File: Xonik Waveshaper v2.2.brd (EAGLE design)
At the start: 55.9 x 21 mm, 78 parts, among them IC1 TL074JT, IC2 TL074JT, IC3 TL074JT, IC4 TL072JT, IC5 4013T, IC6 LM311T, T1 2n3904

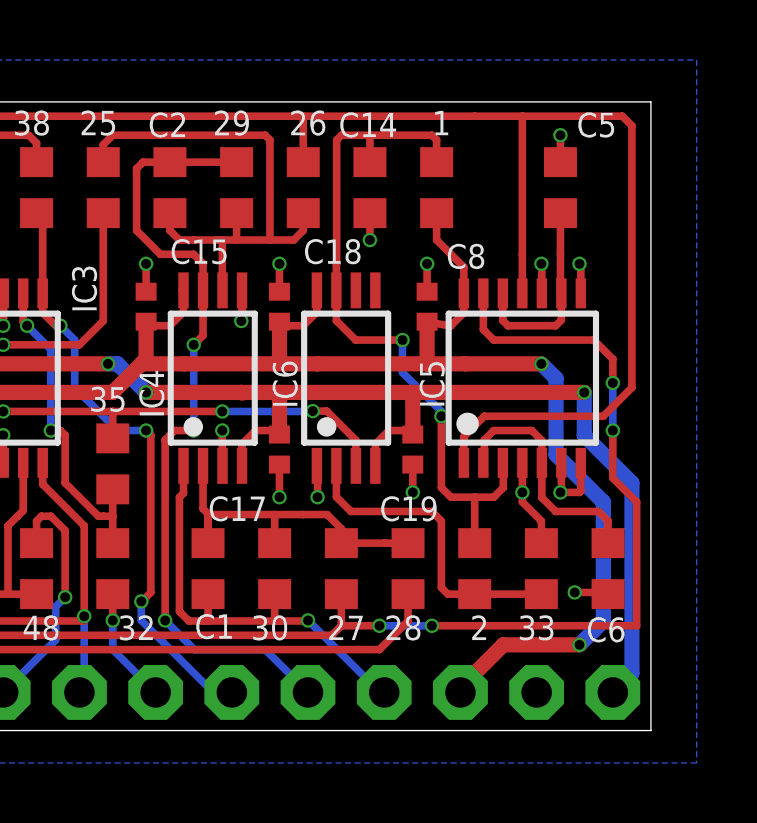
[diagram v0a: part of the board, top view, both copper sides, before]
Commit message: Replaced LM311 with SO08 because TSSOP is sold out at JLCPCB
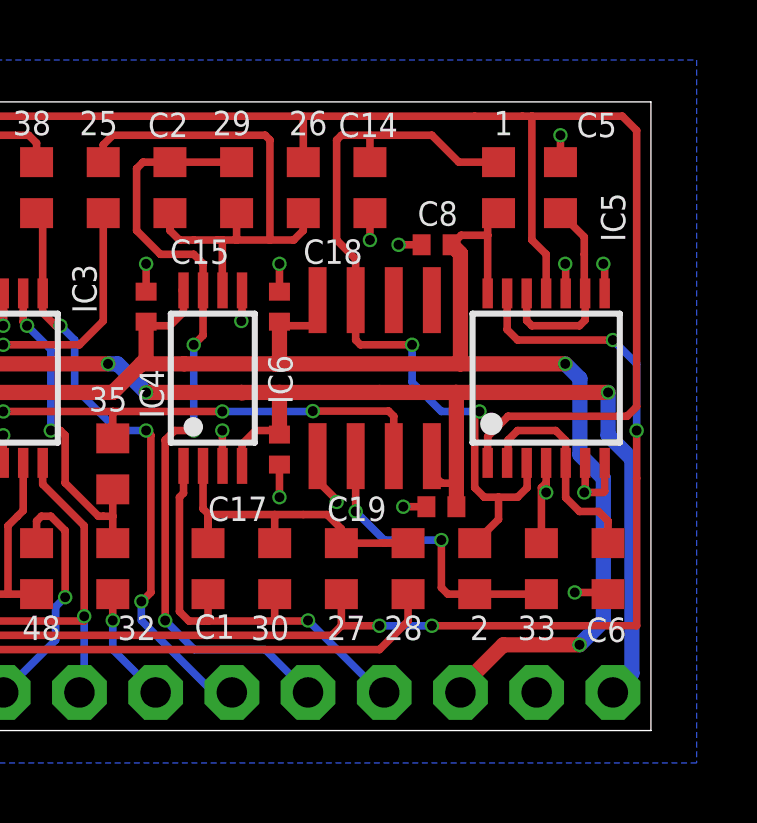
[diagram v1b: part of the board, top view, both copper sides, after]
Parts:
- IC6: value LM311T -> LM311D; device joakim:TSSOP8J -> joakim:SO08J
- moved C19 2.13 mm to (48.9, 7.46), turned to 180 degrees
- moved C8 2.09 mm to (48.7, 16.2), turned to 0 degrees
- moved 1 2.06 mm to (50.8, 18.1)
- moved IC6 0.95 mm to (46.7, 11.7), turned to 0 degrees
- moved IC5 0.79 mm to (52.4, 11.7)
- moved U$1 0.79 mm to (55.1, 11.3)
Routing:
- net -12V: track 77.7 -> 81.2 mm
- net SQR: track 24.0 -> 27.1 mm
- net +12V: track 88.1 -> 90.4 mm
- net SAW: track 39.0 -> 40.4 mm
- net GND: track 45.9 -> 46.7 mm
- net N$31: track 8.14 -> 7.34 mm
- net N$25: track 10.6 -> 10.2 mm, vias 0 -> 2

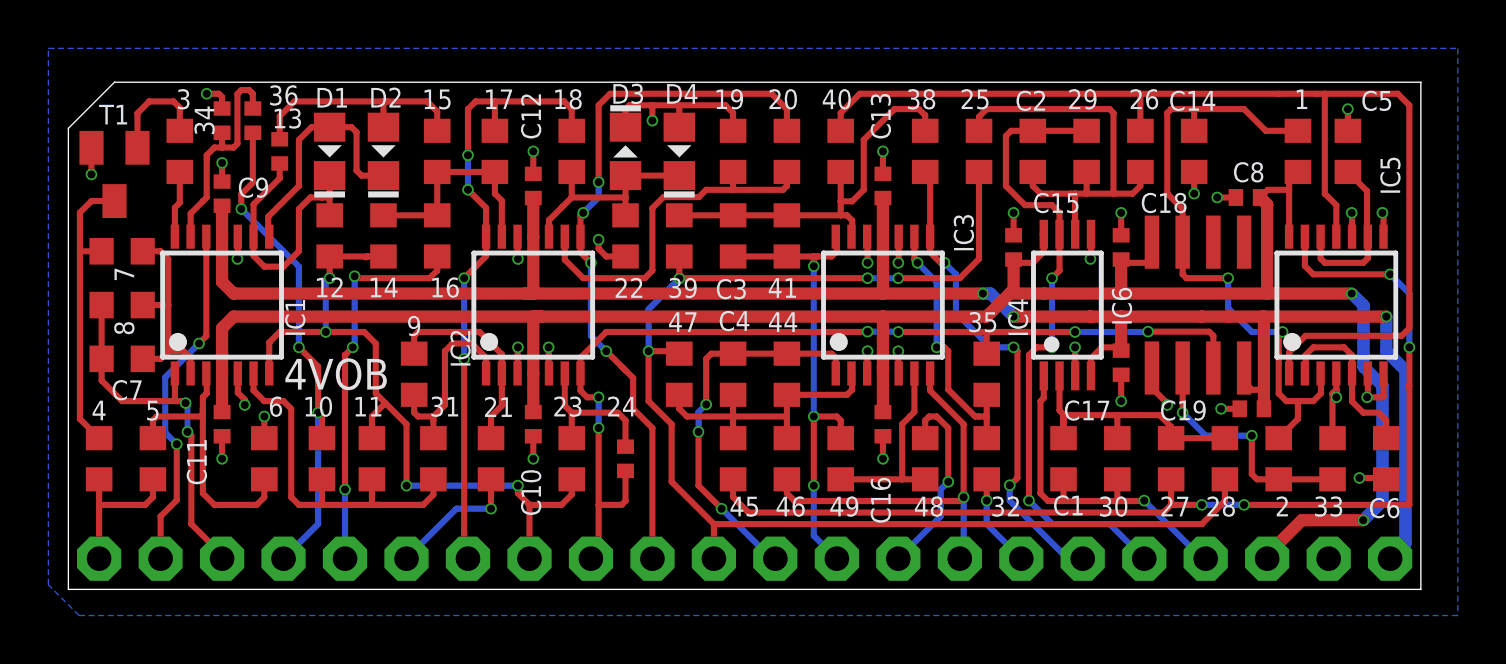
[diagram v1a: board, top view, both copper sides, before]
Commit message: Increased via outer diameter
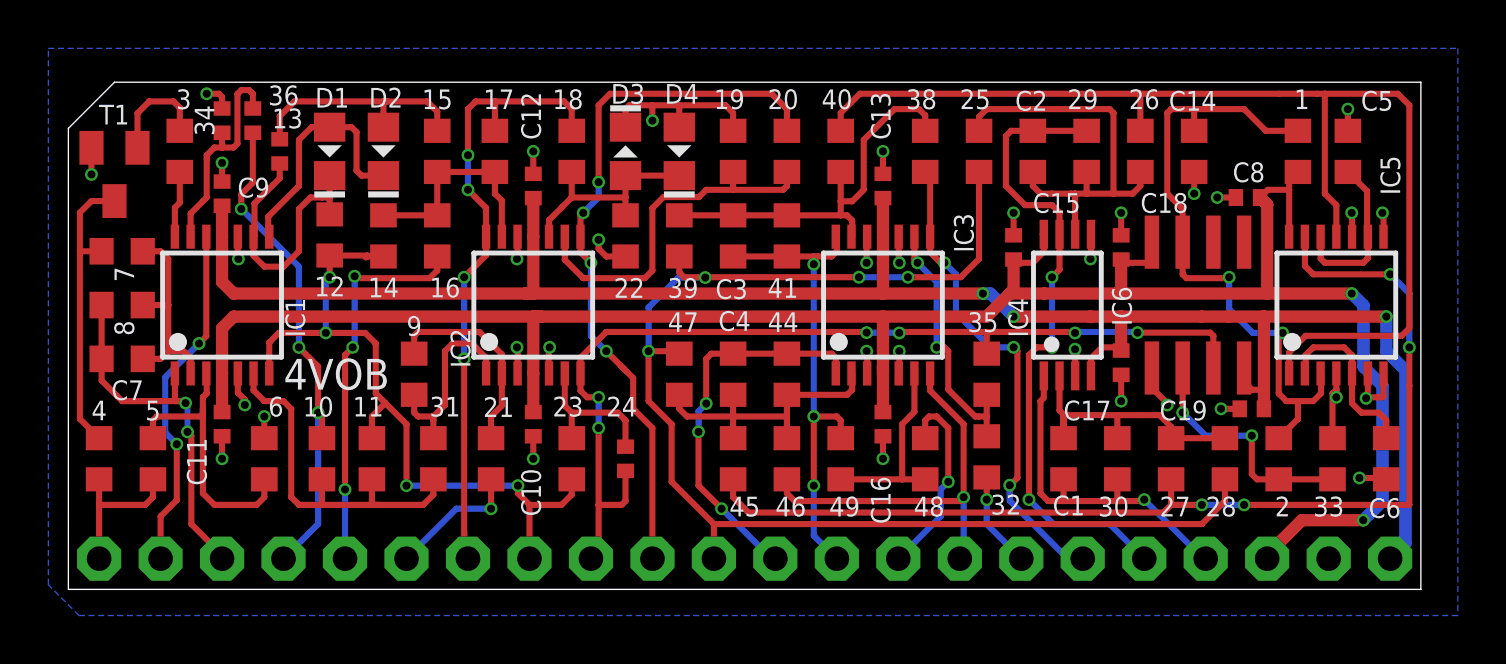
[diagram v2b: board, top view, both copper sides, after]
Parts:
- moved 32 0.08 mm to (37.9, 5.48)
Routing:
- net -5V: track 54.4 -> 55.3 mm
